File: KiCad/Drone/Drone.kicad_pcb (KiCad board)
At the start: 2 copper layers, 91.4 x 57.1 mm, 21 parts, among them J1 ESC, J10 to ESC Power, J11 Conn_01x02_Female, J2 BATTRY, J3 ESP32_LEFT, J4 Raspberry Pi, J5 ESP32_RIGHT, J6 DPS310_LEFT, J7 US-015, J8 MPU9250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

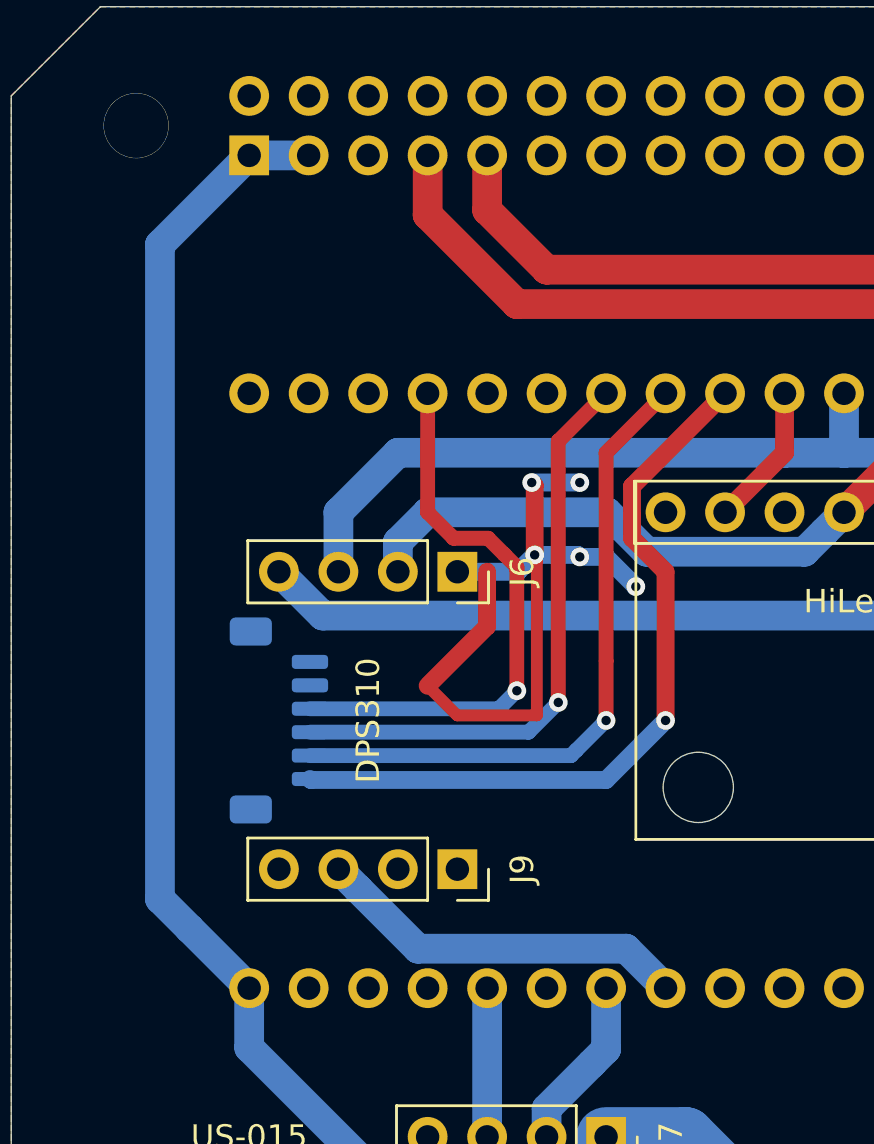
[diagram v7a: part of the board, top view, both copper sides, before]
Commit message: :recycle:ESCの位置を変更
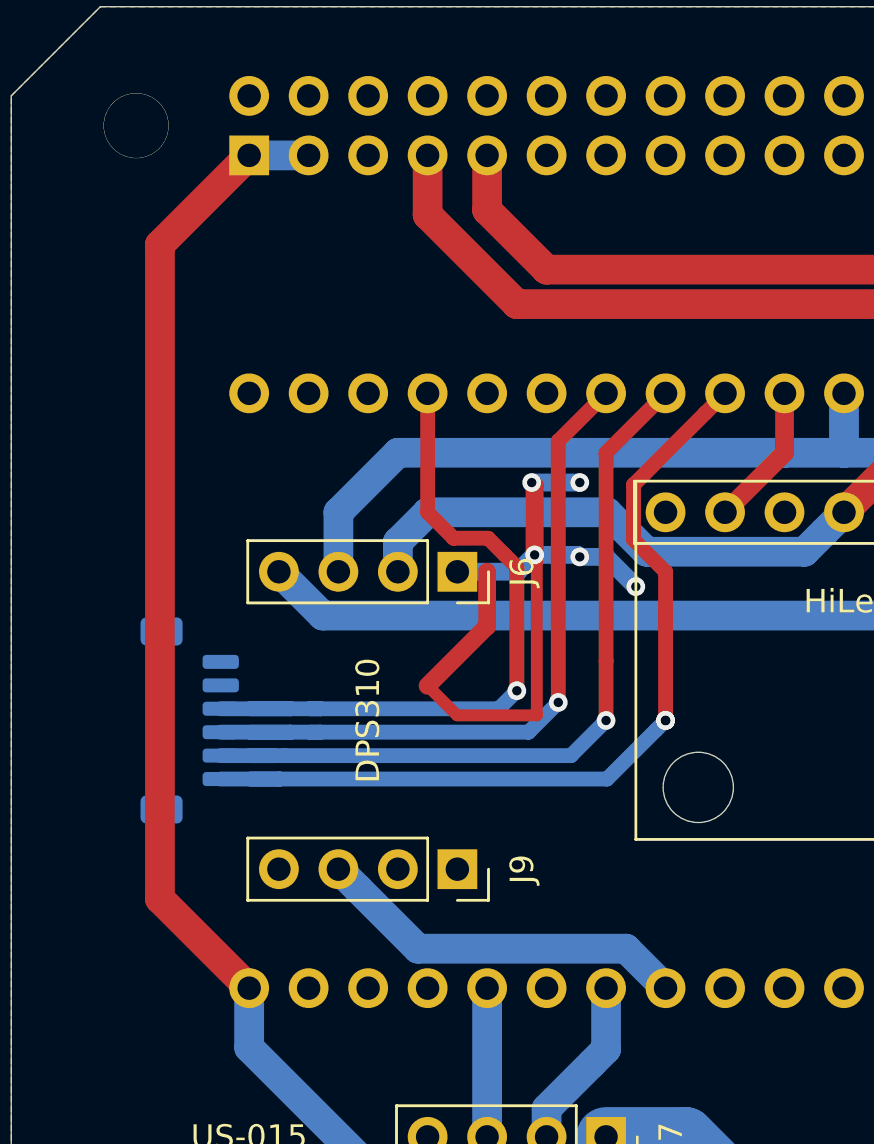
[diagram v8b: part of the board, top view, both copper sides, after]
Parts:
- moved J1 3.81 mm to (99.1, 102.9)
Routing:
- net GPIO4: track 25.2 -> 31.1 mm
- net GPIO15: track 24.3 -> 30.3 mm
- net GPIO17: track 32.5 -> 37.4 mm, vias 1 -> 2
- net GPIO16: track 28.3 -> 33.1 mm
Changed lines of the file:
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@@
     (thickness 1.6)
     (drawings 33)
-    (tracks 311)
+    (tracks 323)
     (zones 0)
     (modules 21)
@@
   (page A4)
   (layers
-    (0 F.Cu signal)
-    (31 B.Cu signal)
+    (0 F.Cu signal hide)
+    (31 B.Cu signal hide)
     (32 B.Adhes user)
     (33 F.Adhes user hide)
@@
   )
   (setup
-    (last_trace_width 2.54)
+    (last_trace_width 0.635)
     (user_trace_width 0.254)
     (user_trace_width 0.508)
@@
   )
   (module Connector_JST:JST_SH_BM06B-SRSS-TB_1x06-1MP_P1.00mm_Vertical (layer B.Cu)
-    (at 102.87 102.87 270)
+    (at 99.06 102.87 270)
     (descr "JST SH series connector, BM06B-SRSS-TB (http://www.jst-mfg.com/product/pdf/eng/eSH.pdf), generated with kicad-footprint-generator")
     (tags "connector JST SH side entry")
@@
   (segment (start 141.726001 124.240001) (end 140.750001 124.240001) (width 2.54) (layer B.Cu) (net 3))
   (segment (start 104.14 78.74) (end 101.6 78.74) (width 1.27) (layer B.Cu) (net 3))
-  (segment (start 99.06 111.76) (end 101.6 114.3) (width 1.27) (layer B.Cu) (net 3))
-  (segment (start 97.79 110.49) (end 99.06 111.76) (width 1.27) (layer B.Cu) (net 3))
-  (segment (start 101.6 78.74) (end 97.79 82.55) (width 1.27) (layer B.Cu) (net 3))
-  (segment (start 97.79 82.55) (end 97.79 110.49) (width 1.27) (layer B.Cu) (net 3))
   (segment (start 155.345 107.576998) (end 155.345 110.23) (width 1.27) (layer F.Cu) (net 3))
   (segment (start 154.863001 107.094999) (end 155.345 107.576998) (width 1.27) (layer F.Cu) (net 3))
@@
   (segment (start 107.95 123.19) (end 116.42 123.19) (width 1.27) (layer B.Cu) (net 3))
   (segment (start 107.95 123.19) (end 101.6 116.84) (width 1.27) (layer B.Cu) (net 3))
+  (segment (start 97.79 110.49) (end 101.6 114.3) (width 1.27) (layer F.Cu) (net 3))
+  (segment (start 101.6 78.74) (end 97.79 82.55) (width 1.27) (layer F.Cu) (net 3))
+  (segment (start 97.79 82.55) (end 97.79 110.49) (width 1.27) (layer F.Cu) (net 3))
   (segment (start 144.78 117.3225) (end 144.6275 117.475) (width 1.27) (layer F.Cu) (net 4))
   (segment (start 144.78 114.3) (end 144.78 117.3225) (width 1.27) (layer F.Cu) (net 4))
@@
   (via (at 158.080343 106.714657) (size 0.8) (drill 0.4) (layers F.Cu B.Cu) (net 5))
   (segment (start 157.48 107.315) (end 158.080343 106.714657) (width 1.27) (layer B.Cu) (net 5))
-  (segment (start 104.195 103.37) (end 113.53 103.37) (width 0.635) (layer B.Cu) (net 6))
   (segment (start 114.8 90.94) (end 114.8 102.1) (width 0.635) (layer F.Cu) (net 6))
   (segment (start 116.84 88.9) (end 114.8 90.94) (width 0.635) (layer F.Cu) (net 6))
   (via (at 114.8 102.1) (size 0.8) (drill 0.4) (layers F.Cu B.Cu) (net 6))
   (segment (start 113.53 103.37) (end 114.8 102.1) (width 0.635) (layer B.Cu) (net 6))
+  (segment (start 103.37 103.37) (end 101.655 103.37) (width 0.635) (layer B.Cu) (net 6))
+  (segment (start 104.64 103.37) (end 113.53 103.37) (width 0.635) (layer B.Cu) (net 6))
+  (segment (start 104.64 103.37) (end 103.37 103.37) (width 0.635) (layer B.Cu) (net 6))
+  (segment (start 104.195 103.37) (end 104.64 103.37) (width 0.635) (layer B.Cu) (net 6))
+  (segment (start 100.385 103.37) (end 103.37 103.37) (width 0.635) (layer B.Cu) (net 6))
   (segment (start 159.56 91.44) (end 147.32 91.44) (width 1.27) (layer B.Cu) (net 7))
   (via (at 147.32 91.44) (size 0.8) (drill 0.4) (layers F.Cu B.Cu) (net 7))
@@
   (segment (start 113.03 96.314198) (end 113.03 96.429513) (width 0.635) (layer F.Cu) (net 26))
   (segment (start 113.03 101.6) (end 112.26 102.37) (width 0.635) (layer B.Cu) (net 26))
-  (segment (start 104.195 102.37) (end 112.26 102.37) (width 0.635) (layer B.Cu) (net 26))
+  (segment (start 104.64 102.37) (end 112.26 102.37) (width 0.635) (layer B.Cu) (net 26))
+  (segment (start 104.195 102.37) (end 104.64 102.37) (width 0.635) (layer B.Cu) (net 26))
+  (segment (start 100.385 102.37) (end 103.37 102.37) (width 0.635) (layer B.Cu) (net 26))
+  (segment (start 104.64 102.37) (end 103.37 102.37) (width 0.635) (layer B.Cu) (net 26))
+  (segment (start 103.37 102.37) (end 101.655 102.37) (width 0.635) (layer B.Cu) (net 26))
   (segment (start 127 93.98) (end 129.54 91.44) (width 1.27) (layer F.Cu) (net 35))
   (segment (start 129.54 91.44) (end 129.54 88.9) (width 1.27) (layer F.Cu) (net 35))
@@
   (segment (start 117.694999 112.614999) (end 108.804999 112.614999) (width 1.27) (layer B.Cu) (net 37))
   (segment (start 119.38 114.3) (end 117.694999 112.614999) (width 1.27) (layer B.Cu) (net 37))
-  (segment (start 115.34 104.37) (end 115.57 104.14) (width 0.635) (layer B.Cu) (net 38))
-  (segment (start 104.195 104.37) (end 115.34 104.37) (width 0.635) (layer B.Cu) (net 38))
   (segment (start 119.38 88.9) (end 116.84 91.44) (width 0.635) (layer F.Cu) (net 38))
   (via (at 116.84 102.87) (size 0.8) (drill 0.4) (layers F.Cu B.Cu) (net 38))
   (segment (start 116.84 100.33) (end 116.84 102.87) (width 0.635) (layer F.Cu) (net 38))
   (segment (start 116.84 91.44) (end 116.84 100.33) (width 0.635) (layer F.Cu) (net 38))
-  (segment (start 116.84 102.87) (end 115.57 104.14) (width 0.635) (layer B.Cu) (net 38))
-  (segment (start 104.235 105.41) (end 104.195 105.37) (width 0.762) (layer B.Cu) (net 49))
-  (segment (start 116.84 105.41) (end 104.235 105.41) (width 0.762) (layer B.Cu) (net 49))
-  (segment (start 121.92 88.9) (end 117.948999 92.871001) (width 0.762) (layer F.Cu) (net 49))
-  (segment (start 117.948999 94.141001) (end 117.948999 95.088999) (width 0.762) (layer F.Cu) (net 49))
-  (segment (start 117.948999 92.871001) (end 117.948999 94.141001) (width 0.762) (layer F.Cu) (net 49))
+  (segment (start 116.84 102.87) (end 115.34 104.37) (width 0.635) (layer B.Cu) (net 38))
+  (segment (start 115.34 104.37) (end 103.1 104.37) (width 0.635) (layer B.Cu) (net 38))
+  (segment (start 100.385 104.37) (end 102.64 104.37) (width 0.635) (layer B.Cu) (net 38))
+  (segment (start 103.1 104.37) (end 102.64 104.37) (width 0.635) (layer B.Cu) (net 38))
+  (segment (start 102.64 104.37) (end 101.655 104.37) (width 0.635) (layer B.Cu) (net 38))
   (via (at 119.38 102.87) (size 0.8) (drill 0.4) (layers F.Cu B.Cu) (net 49))
-  (segment (start 117.948999 95.088999) (end 119.38 96.52) (width 0.762) (layer F.Cu) (net 49))
-  (segment (start 119.38 96.52) (end 119.38 102.87) (width 0.762) (layer F.Cu) (net 49))
-  (segment (start 119.38 102.87) (end 116.84 105.41) (width 0.762) (layer B.Cu) (net 49))
+  (via (at 119.38 102.87) (size 0.8) (drill 0.4) (layers F.Cu B.Cu) (net 49))
+  (segment (start 116.88 105.37) (end 118.980001 103.269999) (width 0.635) (layer B.Cu) (net 49))
+  (segment (start 118.980001 103.269999) (end 119.38 102.87) (width 0.635) (layer B.Cu) (net 49))
+  (segment (start 118.012499 92.807501) (end 121.070001 89.749999) (width 0.635) (layer F.Cu) (net 49))
+  (segment (start 121.070001 89.749999) (end 121.92 88.9) (width 0.635) (layer F.Cu) (net 49))
+  (segment (start 118.012499 95.152499) (end 118.012499 92.807501) (width 0.635) (layer F.Cu) (net 49))
+  (segment (start 119.38 96.52) (end 118.012499 95.152499) (width 0.635) (layer F.Cu) (net 49))
+  (segment (start 119.38 102.87) (end 119.38 96.52) (width 0.635) (layer F.Cu) (net 49))
+  (segment (start 100.385 105.37) (end 102.91 105.37) (width 0.635) (layer B.Cu) (net 49))
+  (segment (start 101.655 105.37) (end 102.91 105.37) (width 0.635) (layer B.Cu) (net 49))
+  (segment (start 102.91 105.37) (end 116.88 105.37) (width 0.635) (layer B.Cu) (net 49))
   (segment (start 134.62 96.52) (end 134.62 93.98) (width 1.27) (layer B.Cu) (net 51))
   (segment (start 142.903002 96.52) (end 144.78 94.643002) (width 1.27) (layer B.Cu) (net 51))
